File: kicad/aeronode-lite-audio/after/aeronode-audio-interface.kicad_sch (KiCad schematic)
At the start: 4 parts, among them J1 Conn_01x06_Pin, J2 Conn_01x08_Pin, J3 Conn_01x10_Pin, J4 Conn_01x06_Pin

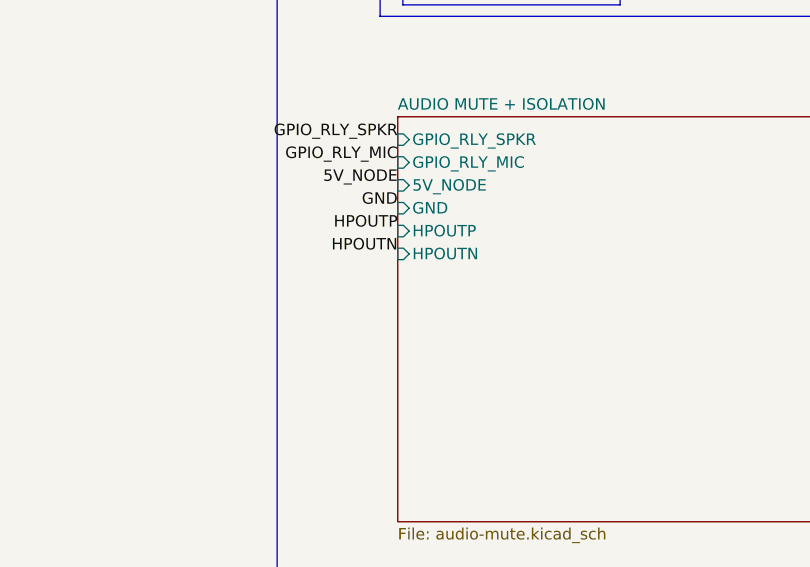
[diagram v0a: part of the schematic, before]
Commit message: [LIMA] audio-mute: ADAU1860 analog IN added - and it needed a second transformer
Peter asked for the ADAU1860 analog out and in connectivity. OUT already
existed (HPOUTP/HPOUTN -> T1 -> R4 -> MIC_LINE) and is now captioned. IN is new:
MIC_LINE -> R9 (2k2) -> MIC_TAP -> T2 (SM-LP-5001) -> AINP2/AINN2.

The load-bearing decision: a capture path tapped straight off the aircraft mic
line into an ADC input would have been a SECOND galvanic crossing, silently
destroying section 11.3's claim that T1 is the only one. So the capture gets
its own transformer. Two transformers, boundary intact.

- R9=2k2 keeps the tap high-Z: ~1.3 dB loading on the pilot's mic to the radio,
  LF corner ~92 Hz. Speech lands ~-41 dBFS, 114 dB SPL near -20 dBFS, so the
  PGA must not run near maximum.
- Codec symbol still deliberately NOT placed: the ADAU1761-vs-1860 choice is
  John's per h1-audio-board-codec-selection.md, and placing a symbol would
  quietly take it. The interface is sheet pins instead.
- ERC 41 = untouched baseline. validate_sheet_pins 0 issues across 8 pins.
  Netlist verified on both sides of the boundary.

FLAGGED, NOT DECIDED: as drawn, muting the mic also deafens AeroNode's own
capture, because K2 shunts the shared node the capture taps. If the wanted
behaviour is "the radio cannot hear the pilot but AeroNode can", K2 must become
a series break with the tap on the headset side - which reopens the DC-thump
question 10.2 closed. On the sheet and in the note.

Scar confirmed twice now: a Konnect-drawn wire with no net label does not
reliably form a net, and validate_wire_connections passes it anyway.

Co-Authored-By: Claude Opus 5 <noreply@anthropic.com>
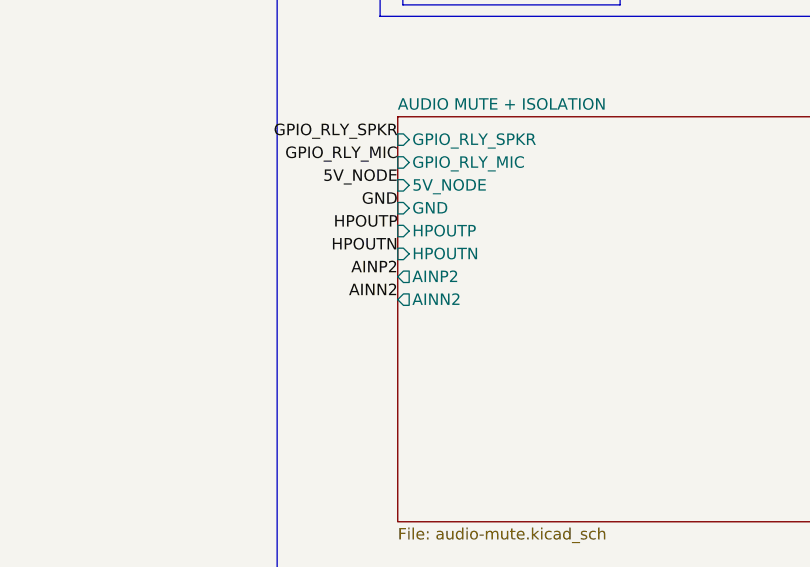
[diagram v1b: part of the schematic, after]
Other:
- sheet AUDIO MUTE + ISOLATION ports: added AINN2, AINP2; removed none
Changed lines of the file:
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@@
+		)
+	)
+	(label "AINP2"
+		(at 115 145.78 180)
+		(effects
+			(font
+				(size 1.27 1.27)
+			)
+			(justify right bottom)
+		)
+	)
+	(label "AINN2"
+		(at 115 148.32 180)
+		(effects
+			(font
+				(size 1.27 1.27)
+			)
+			(justify right bottom)
 		)
 	)
@@
 			(at 115 143.24 180)
 		)
+		(pin "AINP2" output
+			(at 115 145.78 180)
+		)
+		(pin "AINN2" output
+			(at 115 148.32 180)
+		)
 		(instances

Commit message: [LIMA] audio-mute: headset mic is panel-only - capture path removed, and a worse conflict surfaced
Peter ruled the headset electret does not go to AeroNode; a separate analog mic
reaches the CM5 over I2S instead.

Removed from the schematic, not deprecated: R9, T2, MIC_TAP, the AINP2/AINN2
hierarchical labels and their two parent sheet pins. Netlist confirms no AIN*
net and no R9/T2. Both sheets backed up first. ERC 41 = untouched baseline.

The ruling cleans up three things: section 11.3's "T1 is the ONLY crossing" is
literally true again (14 had added a second transformer purely to keep it
honest); open item 12 is CLOSED rather than carried, since with no capture from
this mic the mute-vs-capture conflict cannot arise and 10.2's AC-only shunt
stands; and a transformer plus a resistor come off the BOM.

But it exposes a worse one. With the capture gone, MIC_LINE carries the pilot's
mic AND AeroNode's TTS injected by R4. That TTS reaches the pilot via
HPOUT -> T1 -> R4 -> MIC_LINE -> panel -> intercom -> AC_L/AC_R -> K1 NC. It
arrives through the very contact K1 opens to mute, so muting the headset while
AeroNode speaks cuts the only path AeroNode's voice has and the pilot hears
nothing. K2 compounds it - its shunt sits on MIC_LINE and shorts the injection.

Fix is what John's block diagram drew before the mute-only ruling: make K1 a
CHANGEOVER, NO contact to AeroNode audio rather than AC_GND. Two nets. NOT
taken - Peter ruled mute-only before the injection point existed, so this is
new information rather than grounds to overturn him quietly. On the sheet and
in section 15.

Co-Authored-By: Claude Opus 5 <noreply@anthropic.com>
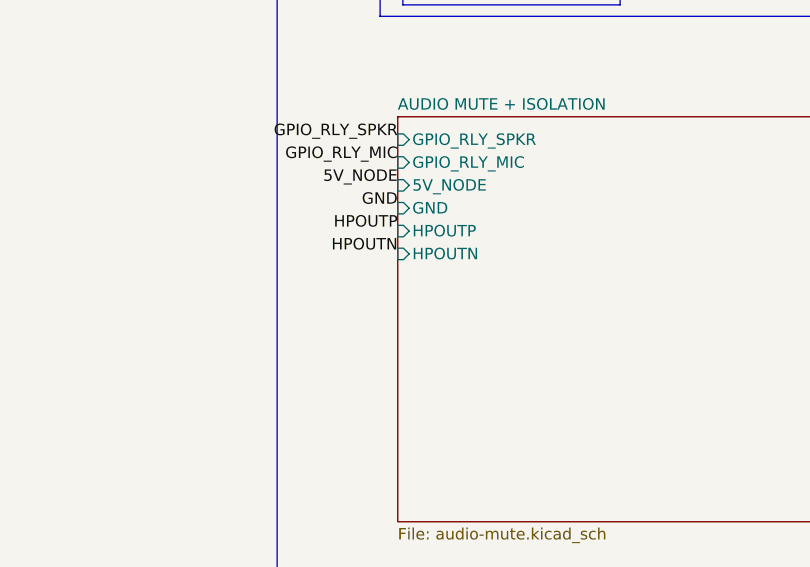
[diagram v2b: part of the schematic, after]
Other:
- sheet AUDIO MUTE + ISOLATION ports: added none; removed AINN2, AINP2
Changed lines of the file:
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@@
-		)
-	)
-	(label "AINP2"
-		(at 115 145.78 180)
-		(effects
-			(font
-				(size 1.27 1.27)
-			)
-			(justify right bottom)
-		)
-	)
-	(label "AINN2"
-		(at 115 148.32 180)
-		(effects
-			(font
-				(size 1.27 1.27)
-			)
-			(justify right bottom)
 		)
 	)
@@
 			(at 115 143.24 180)
 		)
-		(pin "AINP2" output
-			(at 115 145.78 180)
-		)
-		(pin "AINN2" output
-			(at 115 148.32 180)
-		)
 		(instances
